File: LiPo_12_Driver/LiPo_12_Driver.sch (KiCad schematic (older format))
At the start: 32 parts

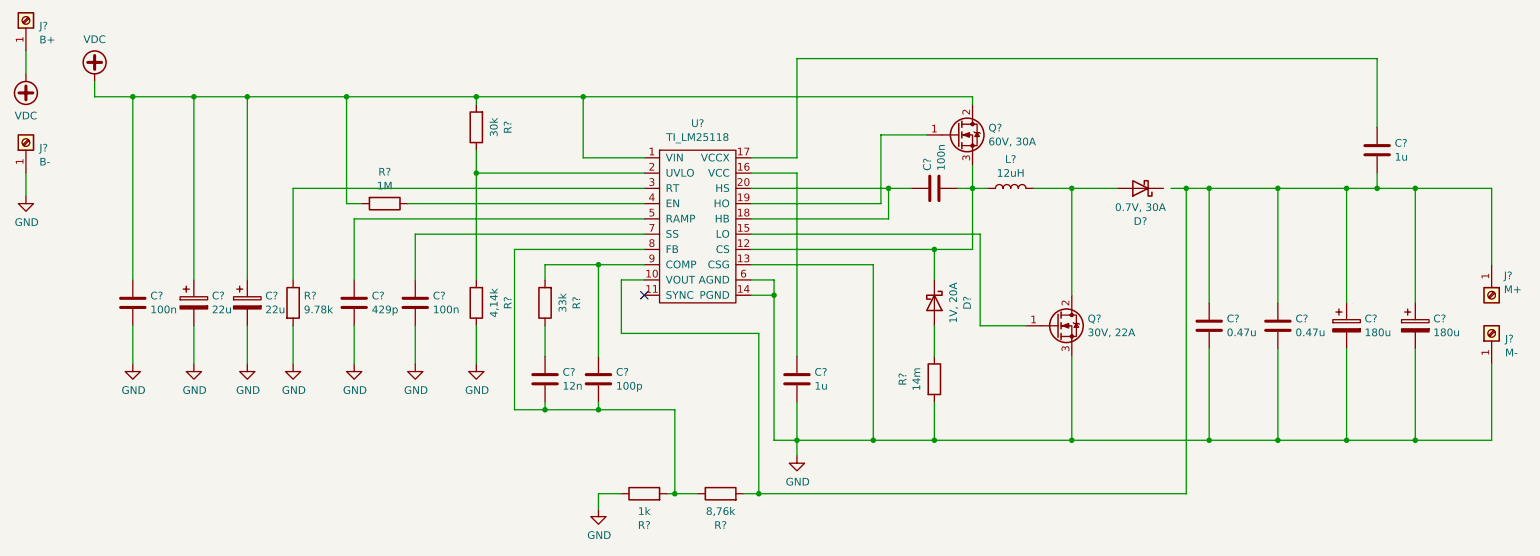
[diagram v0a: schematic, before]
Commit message: Finished LIPO Driver
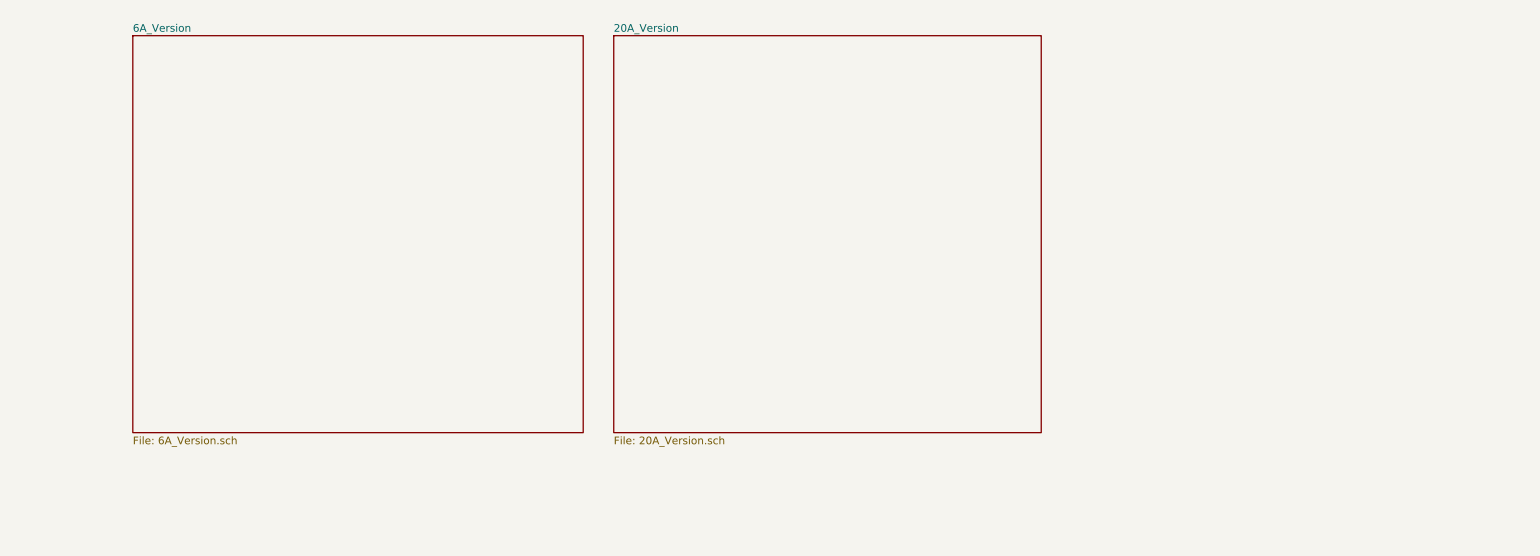
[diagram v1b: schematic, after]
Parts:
- removed C?: 429p, symbol Device:C
- removed C? (x2): 180u, symbol Device:CP
- removed C? (x2): 22u, symbol Device:CP
- removed C? (x3): 100n, symbol Device:C
- removed C? (x2): 1u, symbol Device:C
- removed C?: 12n, symbol Device:C
- removed C?: 100p, symbol Device:C
- removed C? (x2): 0.47u, symbol Device:C
- removed D?: 0.7V, 30A, symbol Device:D_Schottky
- removed D?: 1V, 20A, symbol Device:D_Schottky
- removed J?: M+, symbol Connector:Screw_Terminal_01x01
- removed J?: M-, symbol Connector:Screw_Terminal_01x01
- removed J?: B+, symbol Connector:Screw_Terminal_01x01
- removed J?: B-, symbol Connector:Screw_Terminal_01x01
- removed L?: 12uH, symbol Device:L
- removed Q?: 30V, 22A, symbol Device:Q_NMOS_GDS
- removed Q?: 60V, 30A, symbol Device:Q_NMOS_GDS
- removed R?: 9.78k, symbol Device:R
- removed R?: 1M, symbol Device:R
- removed R?: 4,14k, symbol Device:R
- removed R?: 30k, symbol Device:R
- removed R?: 14m, symbol Device:R
- removed R?: 33k, symbol Device:R
- removed R?: 1k, symbol Device:R
- removed R?: 8,76k, symbol Device:R
- removed U?: TI_LM25118, symbol LiPo_12_Driver:TI_LM25118
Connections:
- no-connect marks 1 -> 0

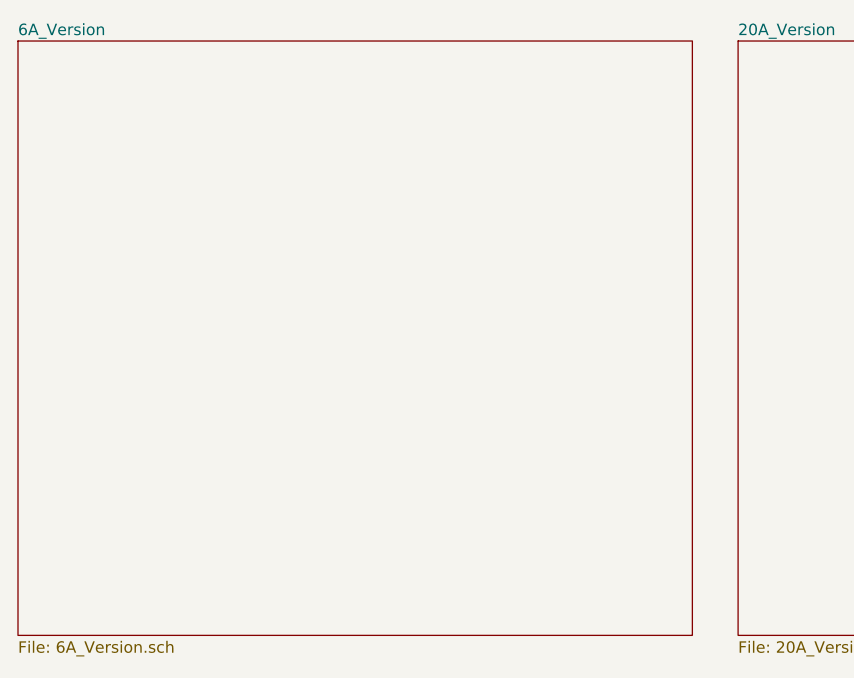
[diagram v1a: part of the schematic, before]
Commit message: Finished LIPO Schematic, started PCB design
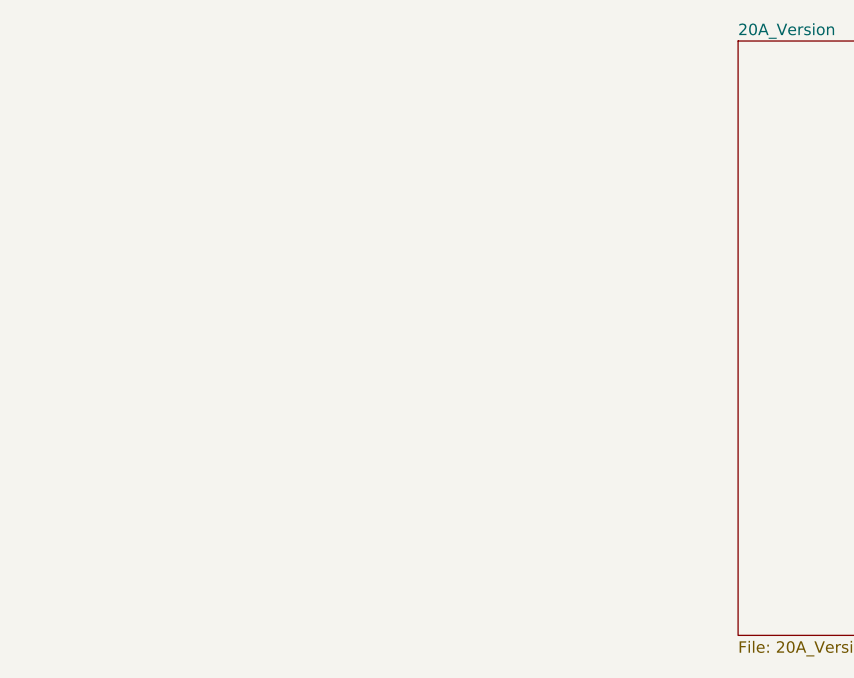
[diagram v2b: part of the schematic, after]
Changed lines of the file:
@@
 $Descr A4 11693 8268
 encoding utf-8
-Sheet 1 3
+Sheet 1 2
 Title ""
 Date ""
@@
 $EndDescr
 $Sheet
-S 1600 2450 2950 2600
-U 6150A5CE
-F0 "6A_Version" 50
-F1 "6A_Version.sch" 50
-$EndSheet
-$Sheet
 S 4750 2450 2800 2600
